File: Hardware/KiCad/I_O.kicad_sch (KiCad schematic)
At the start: 14 parts, among them J1 NC3FAAH-0, J2 NMJ4HFD2, J3 NMJ4HFD2, J4 57PC5F, U3 6N137

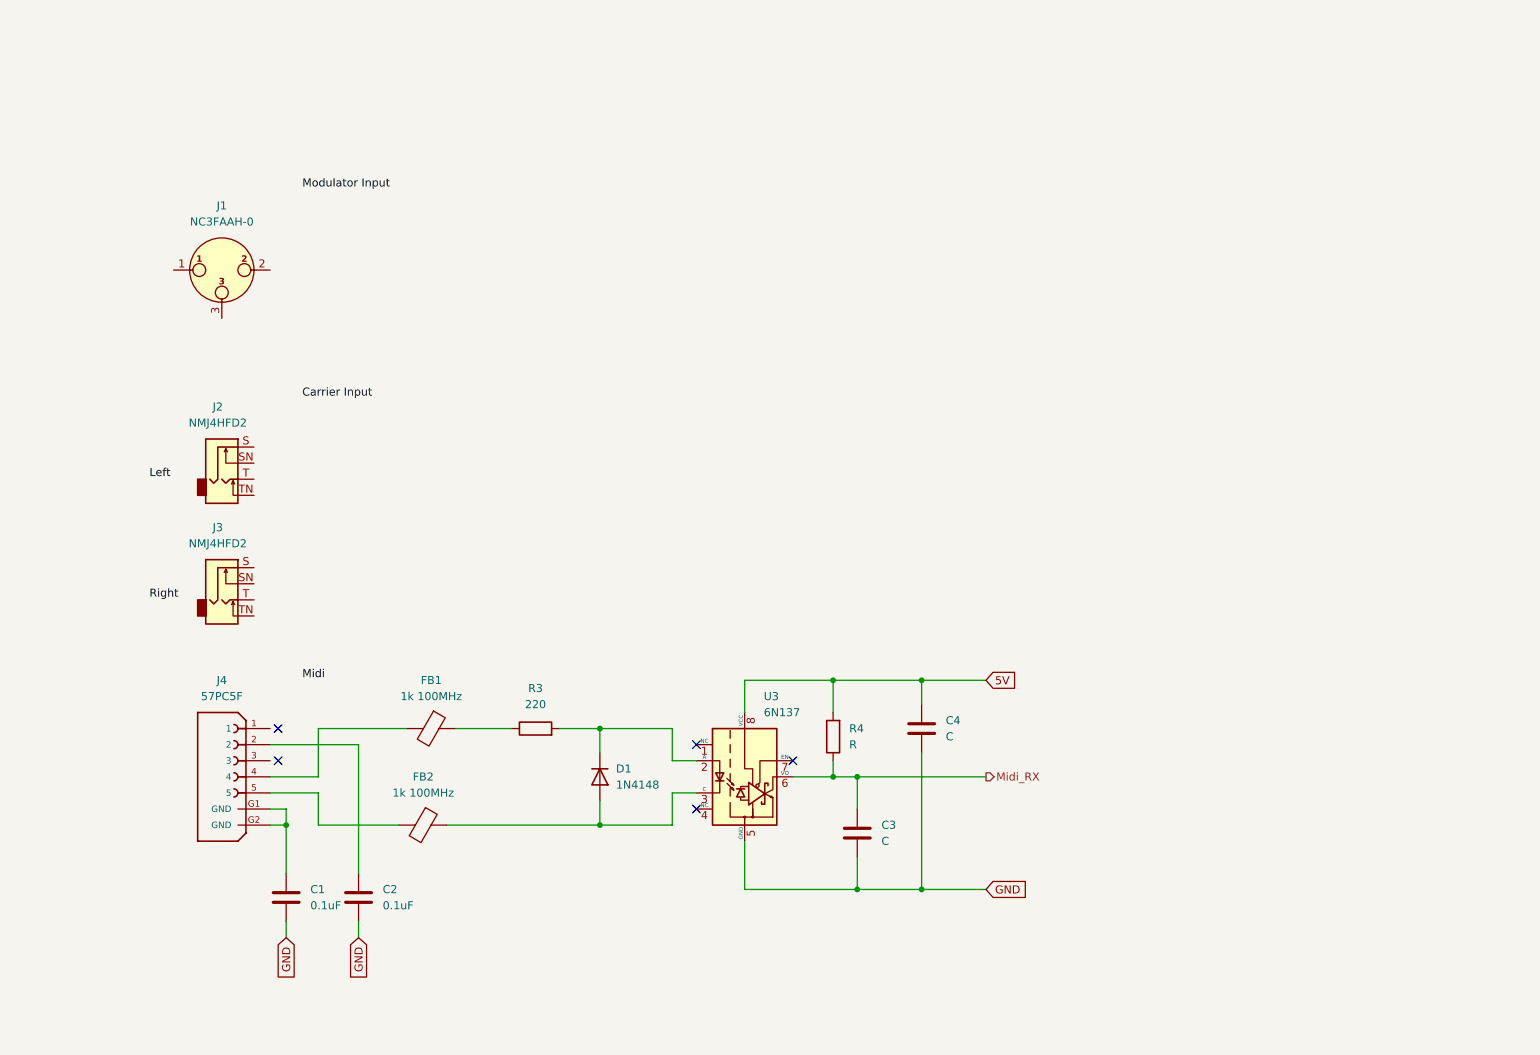
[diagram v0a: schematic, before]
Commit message: Labeled, sheet out from modulator
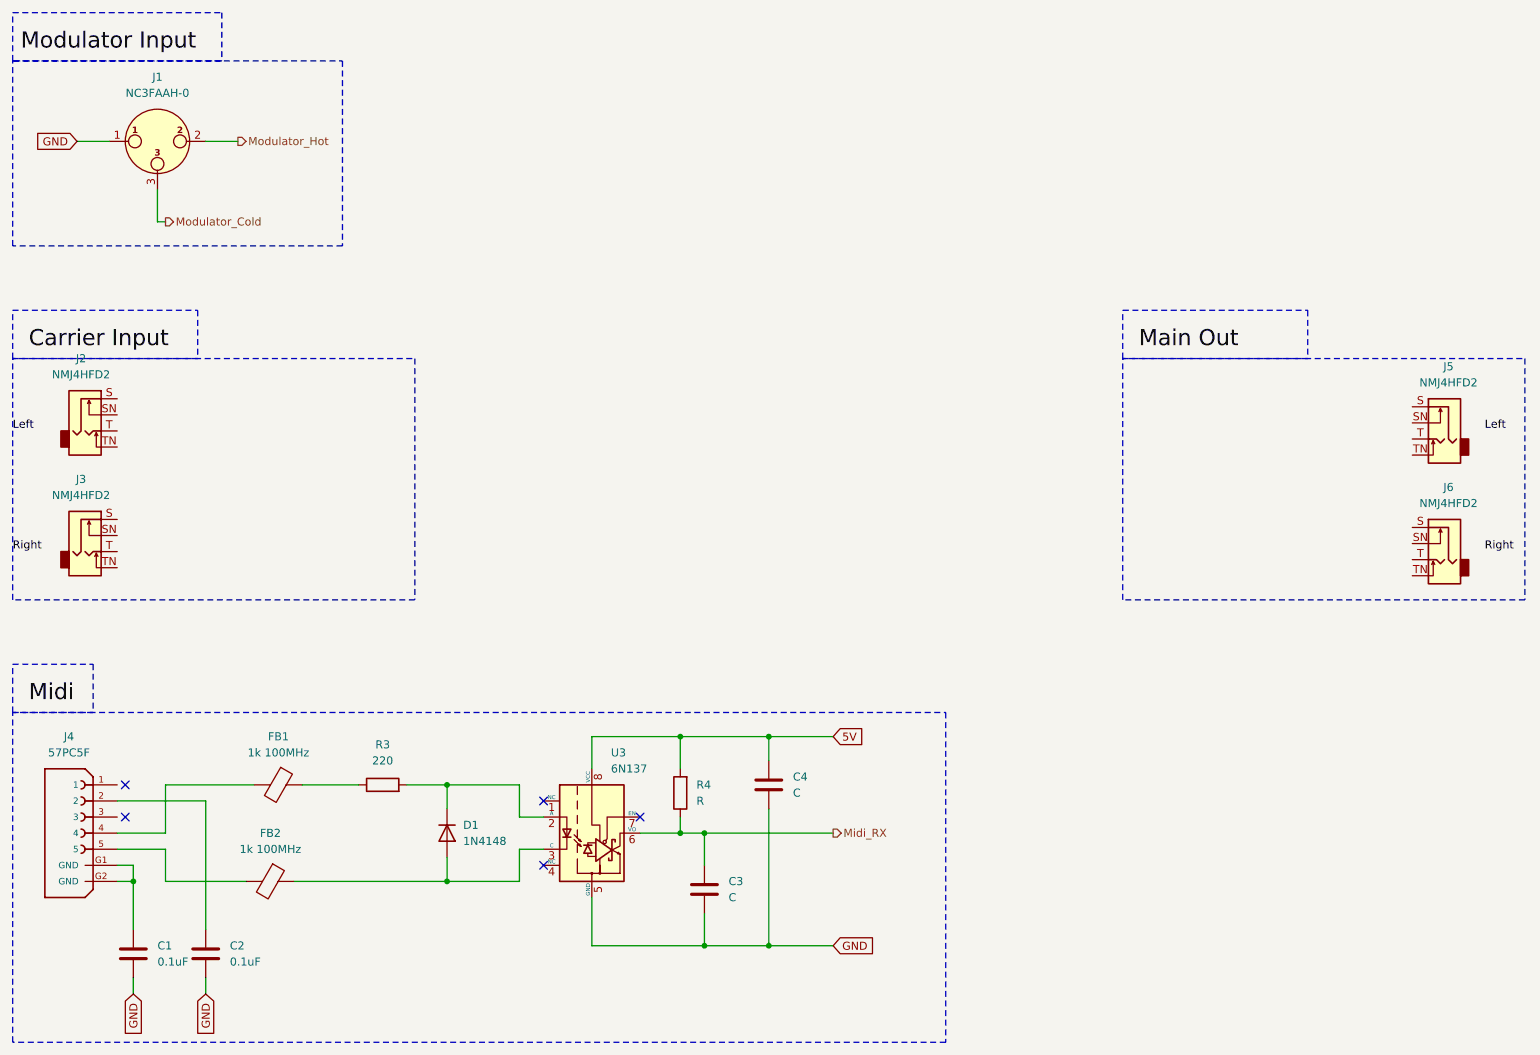
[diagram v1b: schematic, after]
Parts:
- added J5, J6: NMJ4HFD2, Connector_Audio:Jack_6.35mm_Neutrik_NMJ4HFD2_Horizontal, symbol Connector_Audio:NMJ4HFD2
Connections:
- net GND: now also J1.1
- net Modulator_Hot: now reaches J1.2
- net Modulator_Cold: now reaches J1.3
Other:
- moved on the sheet: C1, C2, C3, C4, D1, FB1, FB2, J1, J2, J3, J4, R3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
